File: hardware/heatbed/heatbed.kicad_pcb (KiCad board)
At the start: 2 copper layers, 80 x 80 mm, 2 parts, among them J1 Conn_01x01, J2 Conn_01x01

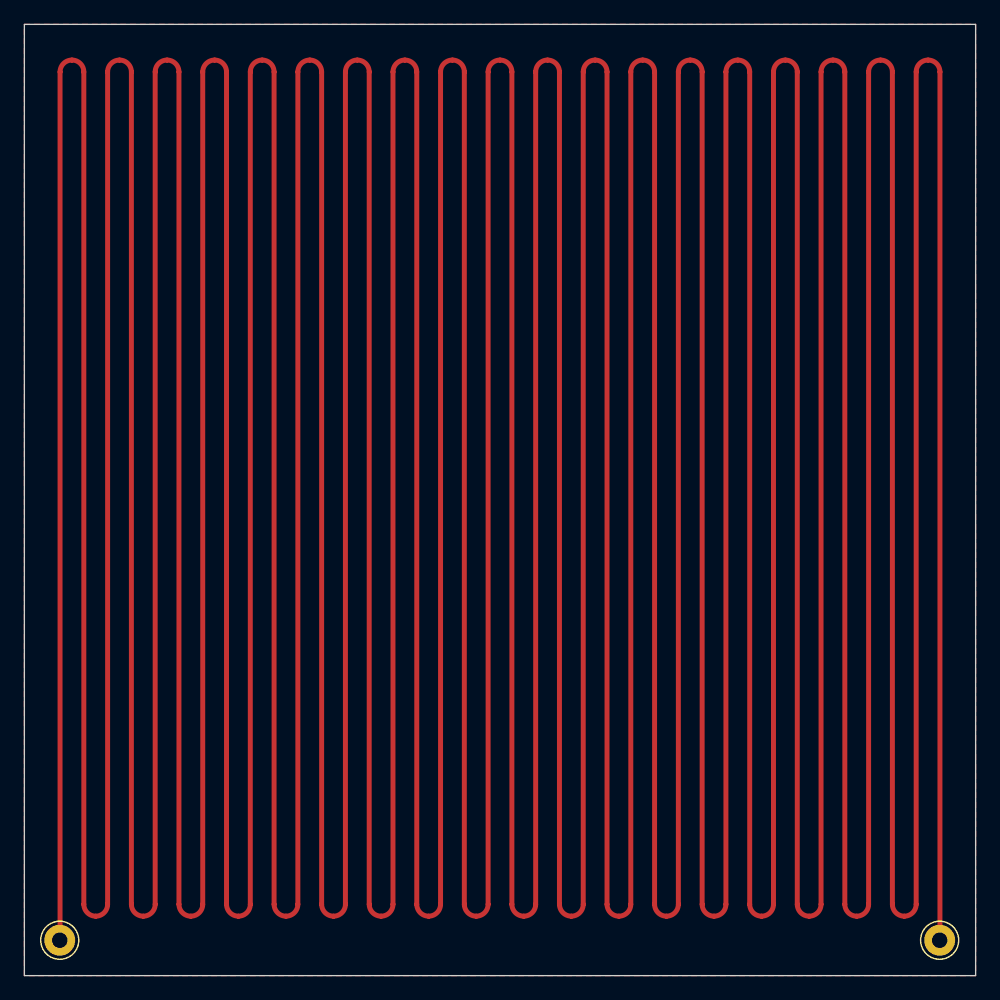
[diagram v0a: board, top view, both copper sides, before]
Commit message: Improve hot plate PCB design
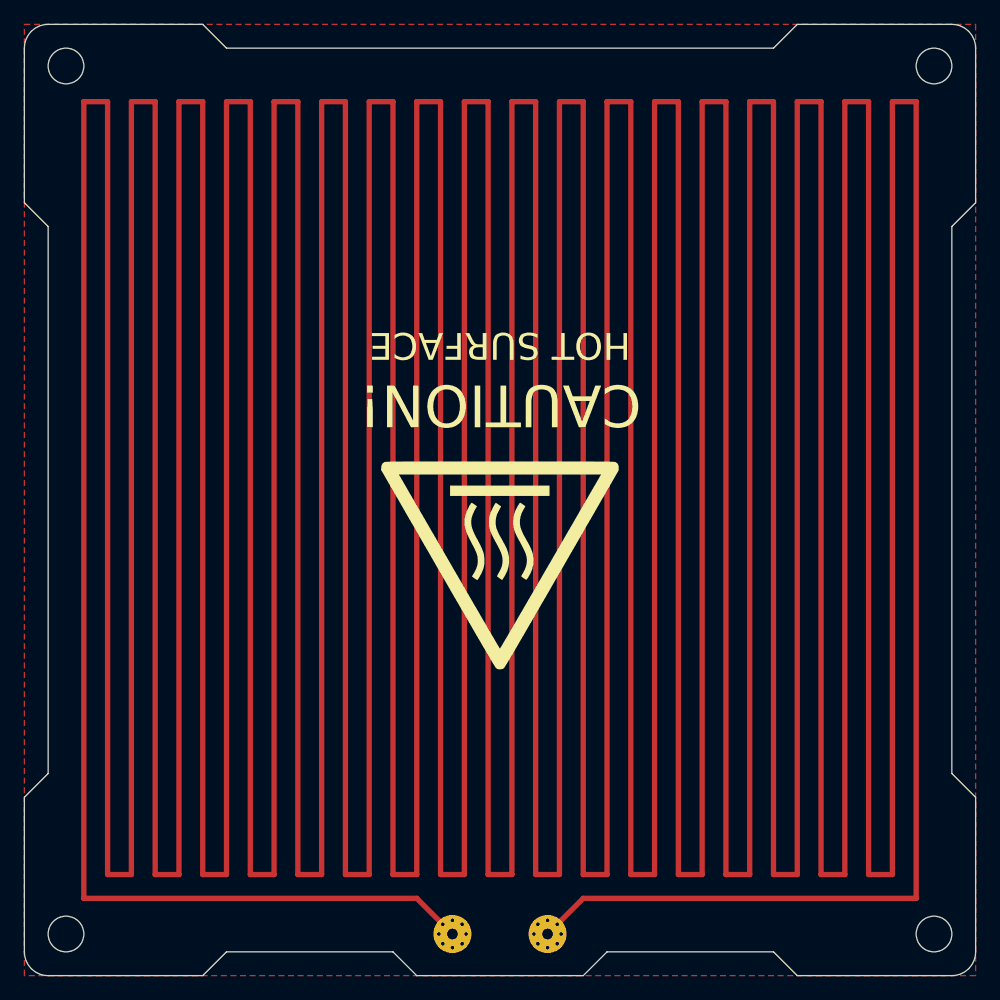
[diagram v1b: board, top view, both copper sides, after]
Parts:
- added G***: LOGO, Local_Library:Hot_Surface_Sign_20mm, F.Cu at (143.0, 101.5)
- added G***: LOGO, Local_Library:Hot_Surface_Sign_20mm, B.Cu at (143.0, 101.5)
- added H1: 3mm, MountingHole:MountingHole_3mm, F.Cu at (106.5, 132.5)
- added H2: 3mm, MountingHole:MountingHole_3mm, F.Cu at (179.5, 132.5)
- added H3: 3mm, MountingHole:MountingHole_3mm, F.Cu at (179.5, 59.5)
- added H4: 3mm, MountingHole:MountingHole_3mm, F.Cu at (106.5, 59.5)
- J1, J2: footprint Connector_Pin:Pin_D1.3mm_L11.0mm -> Local_Library:Pogo_Pad
- moved J1 33.0 mm to (139.0, 132.5)
- moved J2 33.0 mm to (147.0, 132.5)
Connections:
- J1 pad 1: (no net) -> Net-(J1-Pin_1)
- J2 pad 1: (no net) -> Net-(J1-Pin_1)
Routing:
- net (no net): track 2779.3 -> 0.00 mm
- net Net-(J1-Pin_1): track 0.00 -> 2478.5 mm
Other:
- outline, holes or cut-outs redrawn
- board text added: "CAUTION!"
- board text added: "HOT SURFACE"
- board text added: "THIS SIDE UP"
